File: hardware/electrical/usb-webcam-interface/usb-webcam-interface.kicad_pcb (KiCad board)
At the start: 2 copper layers, 3 parts

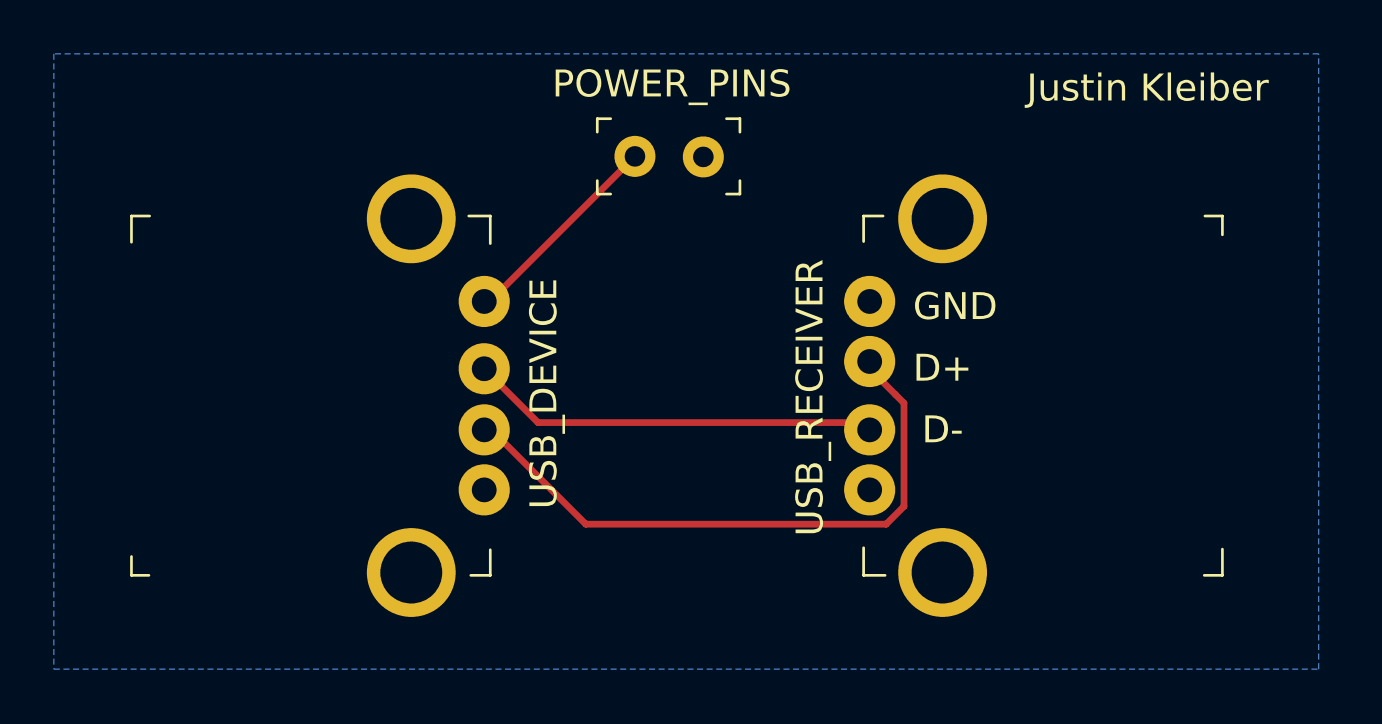
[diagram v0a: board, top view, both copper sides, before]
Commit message: Makes initial project for drivetrain schematic.
Adds tests for encoders, including tracking loop for velocity estimates
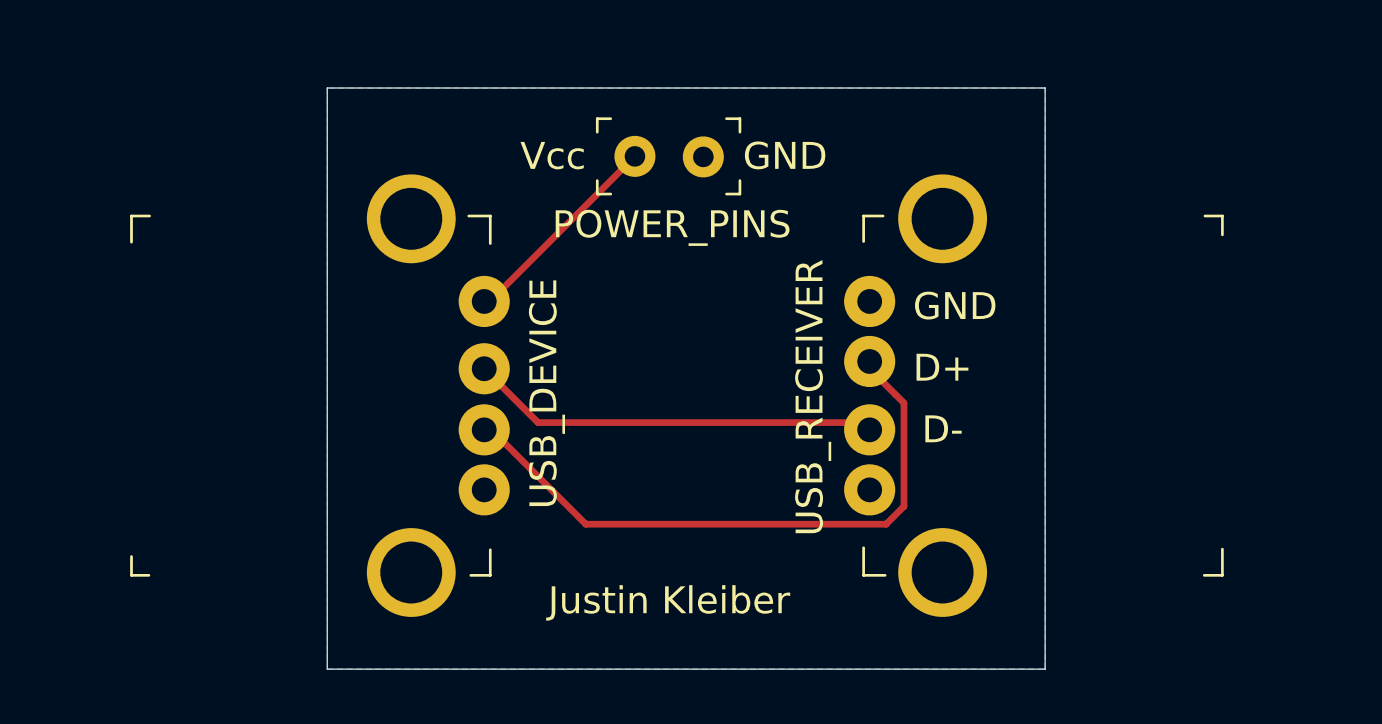
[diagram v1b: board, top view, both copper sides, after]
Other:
- board outline added: 26.7 x 21.6 mm
- board text added: "Vcc"
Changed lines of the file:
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@@
   (general
     (thickness 1.6)
-    (drawings 4)
+    (drawings 10)
     (tracks 11)
     (zones 0)
@@
   (module digikey-footprints:PinHeader_1x2_P2.54mm (layer F.Cu)
     (at 86.36 66.04)
-    (fp_text reference POWER_PINS (at 1.37 -2.69) (layer F.SilkS)
+    (fp_text reference POWER_PINS (at 1.37 2.54) (layer F.SilkS)
       (effects (font (size 1 1) (thickness 0.15)))
     )
@@
       (net 2 "Net-(POWER_PINS1-Pad1)"))
   )
+  (gr_text Vcc (at 83.32 66.04) (layer F.SilkS)
+    (effects (font (size 1 1) (thickness 0.15)))
+  )
+  (gr_text "GND\n" (at 91.94 66.04) (layer F.SilkS)
+    (effects (font (size 1 1) (thickness 0.15)))
+  )
+  (gr_line (start 74.93 85.09) (end 74.93 63.5) (layer Edge.Cuts) (width 0.05))
+  (gr_line (start 101.6 85.09) (end 74.93 85.09) (layer Edge.Cuts) (width 0.05))
+  (gr_line (start 101.6 63.5) (end 101.6 85.09) (layer Edge.Cuts) (width 0.05))
+  (gr_line (start 74.93 63.5) (end 101.6 63.5) (layer Edge.Cuts) (width 0.05))
   (gr_text D- (at 97.79 76.2) (layer F.SilkS)
     (effects (font (size 1 1) (thickness 0.15)))
@@
     (effects (font (size 1 1) (thickness 0.15)))
   )
-  (gr_text "Justin Kleiber" (at 105.41 63.5) (layer F.SilkS)
+  (gr_text "Justin Kleiber" (at 87.63 82.55) (layer F.SilkS)
     (effects (font (size 1 1) (thickness 0.15)))
   )
@@
     (polygon
       (pts
-        (xy 111.76 62.23) (xy 64.77 62.23) (xy 64.77 85.09) (xy 111.76 85.09)
+        (xy 101.6 63.5) (xy 74.93 63.5) (xy 74.93 85.09) (xy 101.6 85.09)
       )
     )
